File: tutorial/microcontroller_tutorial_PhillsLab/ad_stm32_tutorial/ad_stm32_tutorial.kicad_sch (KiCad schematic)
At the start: 29 parts, among them J1 USB_C_Receptacle_USB2.0_16P, J2 TagConnect_TC2030-NL, J3 Conn_01x06, U2 STM32F042G6Ux, Y2 Crystal_GND24

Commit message: Started PCB Layout of power section
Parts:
- FB1: footprint Inductor_SMD:L_6.3x6.3_H3 -> Inductor_SMD:L_0603_1608Metric
- J3: footprint Connector_JST:JST_XH_S6B-XH-A_1x06_P2.50mm_Horizontal -> Connector_JST:JST_EH_S6B-EH_1x06_P2.50mm_Horizontal
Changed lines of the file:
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@@
 			)
 		)
-		(property "Footprint" "Connector_JST:JST_XH_S6B-XH-A_1x06_P2.50mm_Horizontal"
+		(property "Footprint" "Connector_JST:JST_EH_S6B-EH_1x06_P2.50mm_Horizontal"
 			(at 162.56 157.48 0)
 			(effects
@@
 			)
 		)
-		(property "Footprint" "Inductor_SMD:L_6.3x6.3_H3"
+		(property "Footprint" "Inductor_SMD:L_0603_1608Metric"
 			(at 95.25 33.528 90)
 			(effects

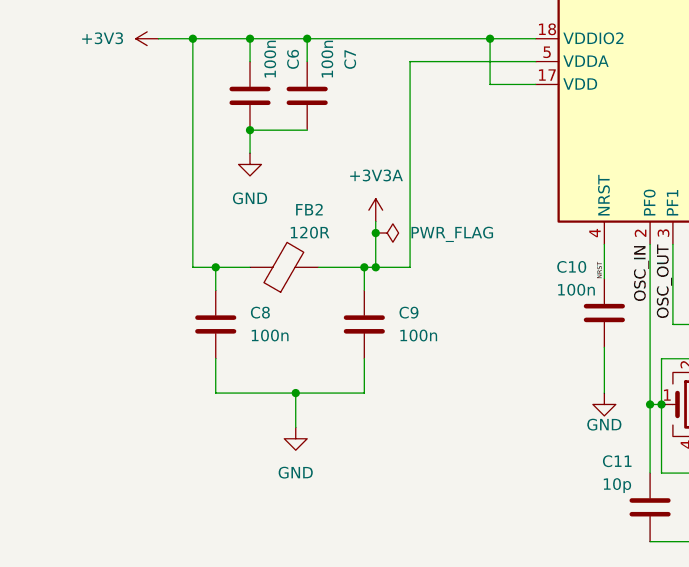
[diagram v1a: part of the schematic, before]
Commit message: Started adding MCU (STM32F4) and it's components
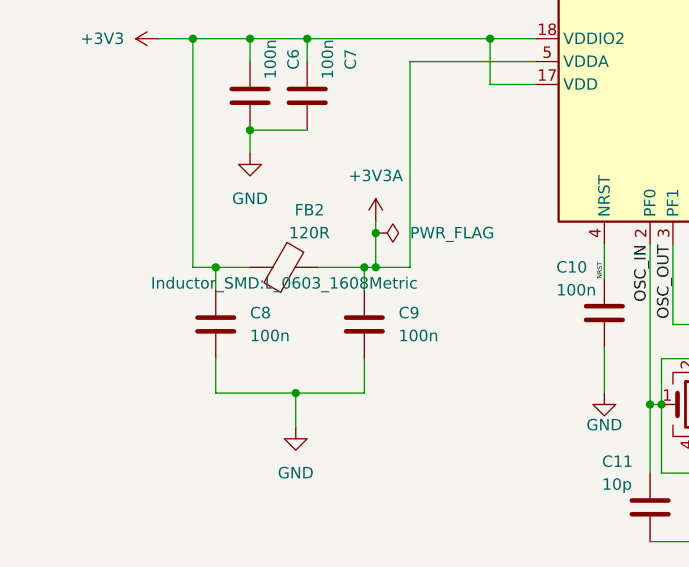
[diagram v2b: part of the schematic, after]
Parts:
- FB2: footprint Inductor_SMD:L_6.3x6.3_H3 -> Inductor_SMD:L_0603_1608Metric
- L1: footprint Inductor_SMD:NRH2412T2R2MNGH -> Inductor_SMD:L_Taiyo-Yuden_NR-24xx
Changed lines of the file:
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@@
 			)
 		)
-		(property "Footprint" "Inductor_SMD:L_6.3x6.3_H3"
+		(property "Footprint" "Inductor_SMD:L_0603_1608Metric"
 			(at 52.07 150.368 90)
 			(effects
@@
 					(size 1.27 1.27)
 				)
-				(hide yes)
 			)
 		)
@@
 			)
 		)
-		(property "Footprint" "Inductor_SMD:NRH2412T2R2MNGH"
+		(property "Footprint" "Inductor_SMD:L_Taiyo-Yuden_NR-24xx"
 			(at 185.42 127.94 0)
 			(effects

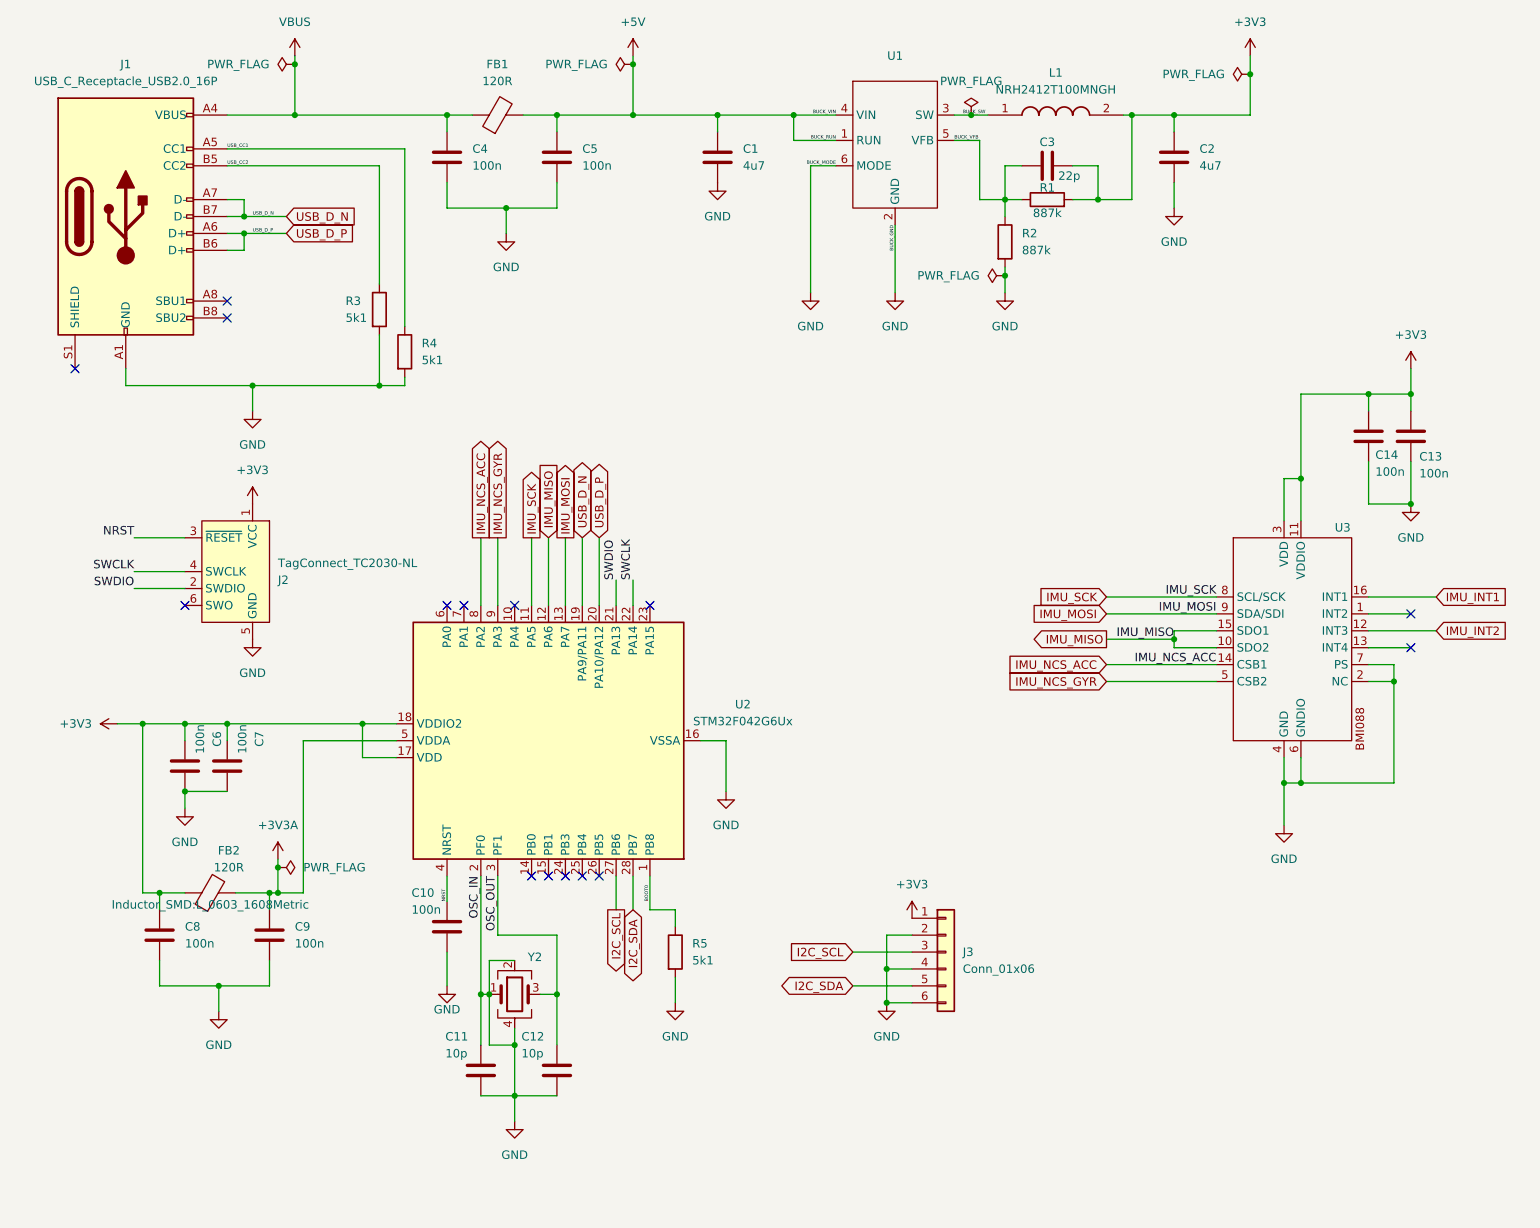
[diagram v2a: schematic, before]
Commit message: Finished placement of all the components
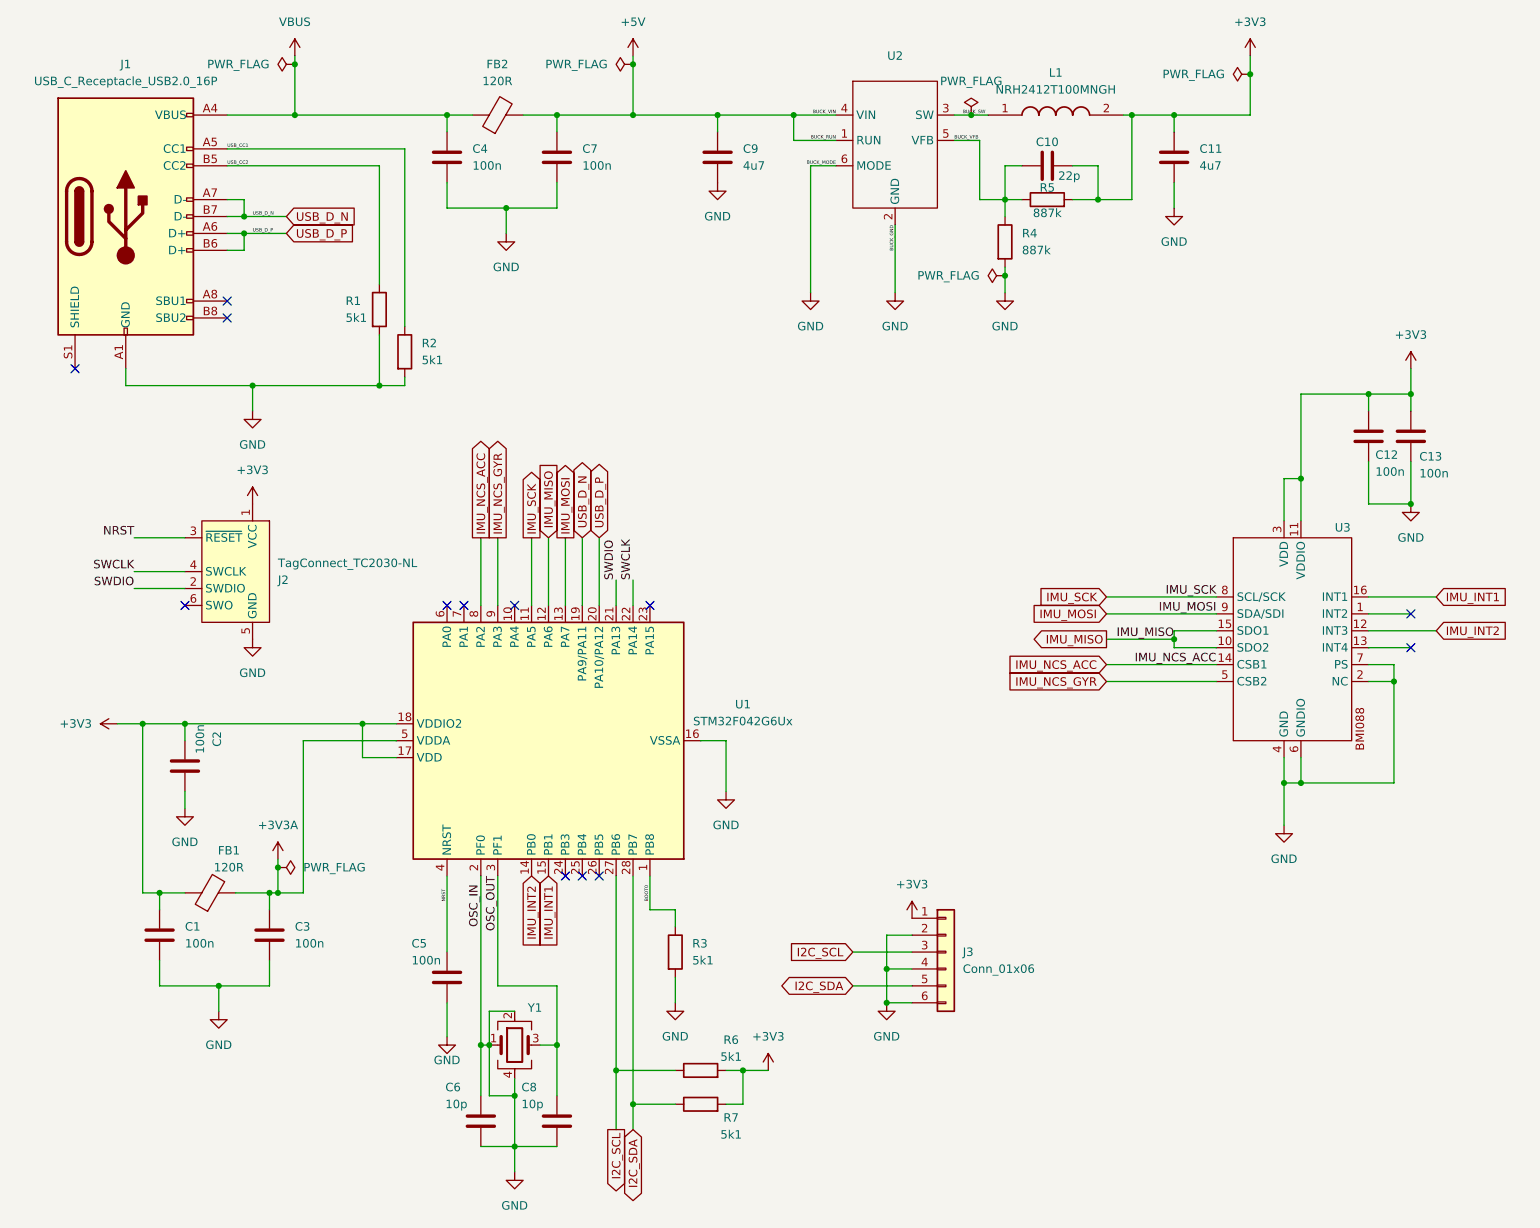
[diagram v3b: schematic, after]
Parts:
- removed C7: 100n, Capacitor_SMD:C_0603_1608Metric, symbol Device:C
- added R6, R7: 5k1, Resistor_SMD:R_0603_1608Metric, symbol Device:R
- J3: footprint Connector_JST:JST_EH_S6B-EH_1x06_P2.50mm_Horizontal -> Connector_JST:JST_GH_SM06B-GHS-TB_1x06-1MP_P1.25mm_Horizontal
- renumbered C8 to C1, C3 to C10, C2 to C11, C14 to C12, C6 to C2, C9 to C3, C10 to C5, C11 to C6, C5 to C7, C12 to C8, C1 to C9, FB2 to FB1, FB1 to FB2, R3 to R1, R4 to R2, R5 to R3, R2 to R4, R1 to R5, U2 to U1, U1 to U2, Y2 to Y1
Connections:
- net +3V3: now also R6.2, R7.2
- net I2C_SCL: now also R6.1
- net I2C_SDA: now also R7.1
- net IMU_INT1: now also U1.15 (PB1)
- net IMU_INT2: now also U1.14 (PB0)
- no-connect marks 15 -> 13
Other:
- moved on the sheet: C5, C6, C8, Y1

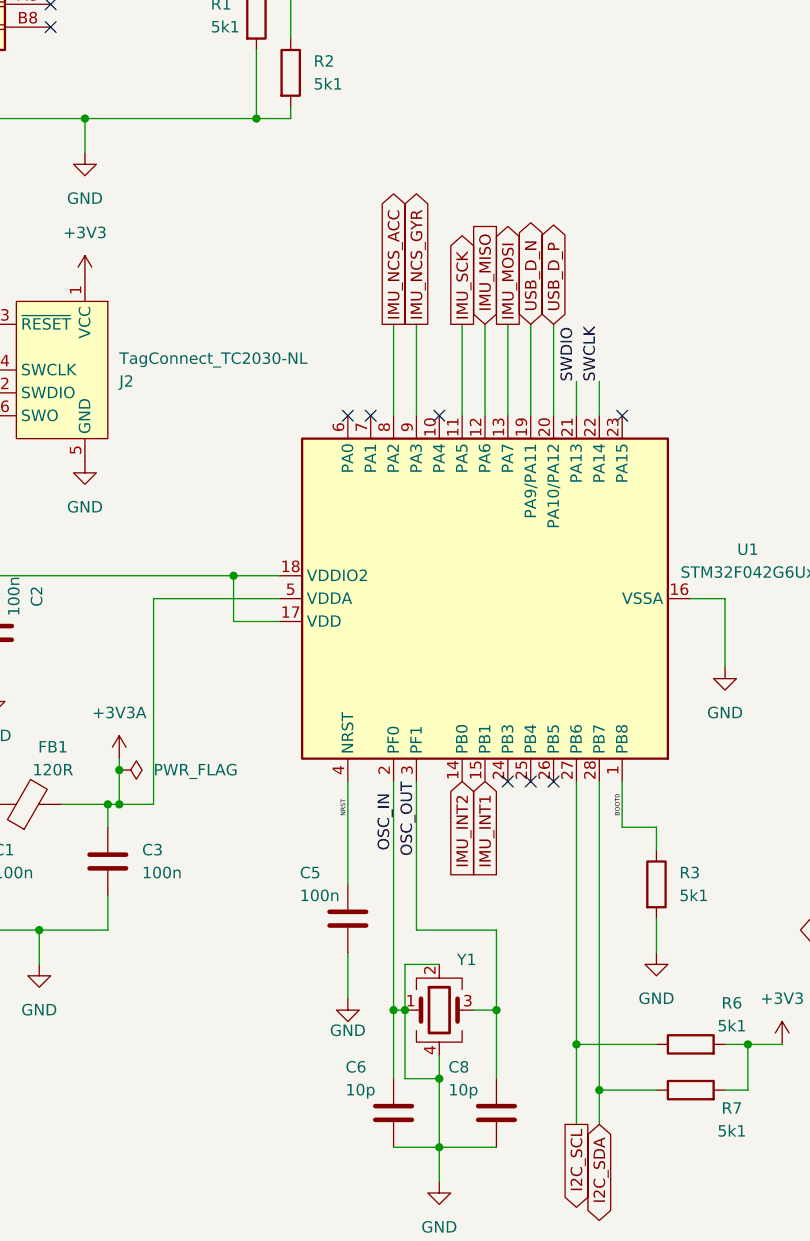
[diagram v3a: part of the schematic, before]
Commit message: Added all the traces and connecting Via's. Check out ViaStitching tool on github
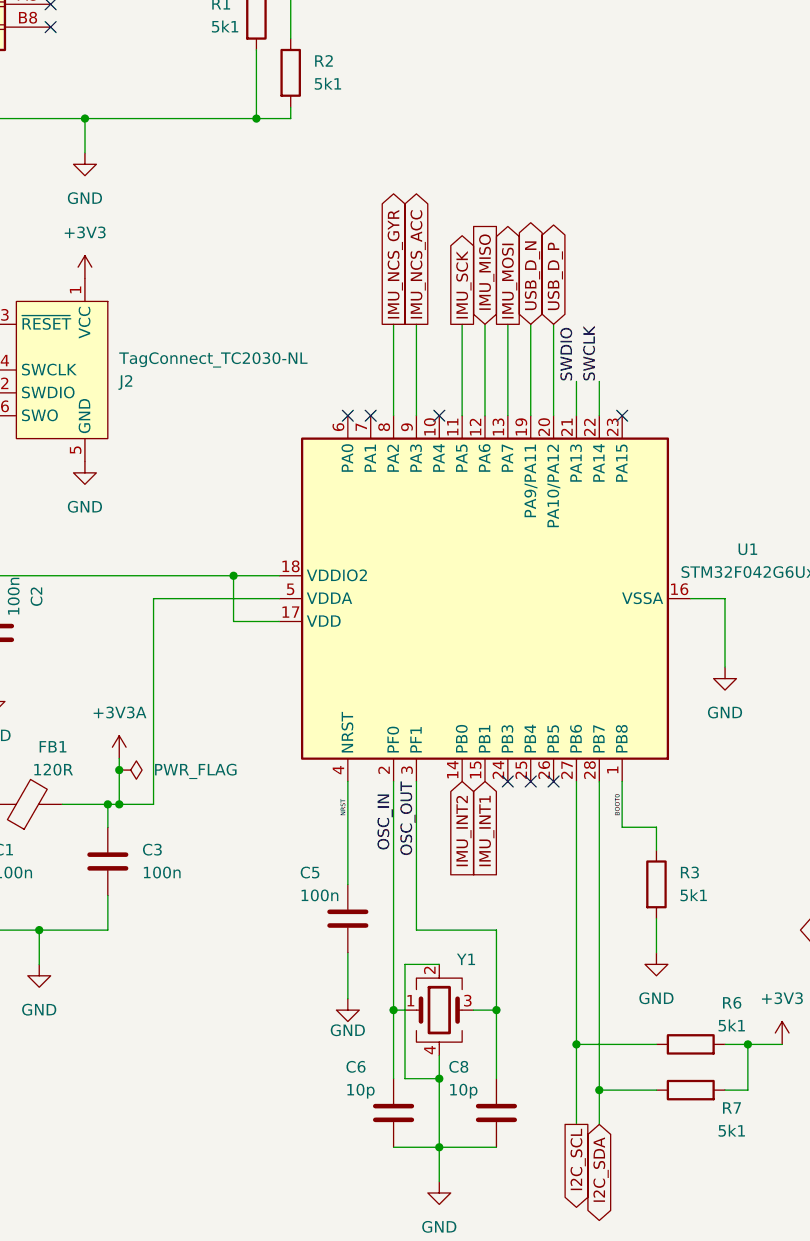
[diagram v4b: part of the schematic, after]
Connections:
- net GND: no longer C6.1, U1.2 (PF0), Y1.1
- net IMU_NCS_ACC: now also U1.9 (PA3); no longer U1.8 (PA2)
- net IMU_NCS_GYR: now also U1.8 (PA2); no longer U1.9 (PA3)
- new net OSC_IN: C6.1, U1.2 (PF0), Y1.1
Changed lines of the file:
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@@
-	)
-	(junction
-		(at 93.98 171.45)
-		(diameter 0)
-		(color 0 0 0 0)
 	)
 	(junction
@@
 	(wire
 		(pts
-			(xy 93.98 171.45) (xy 93.98 179.07)
+			(xy 93.98 166.37) (xy 93.98 179.07)
 		)
 		(stroke
@@
 		(pts
 			(xy 186.69 114.3) (xy 203.2 114.3)
-		)
-		(stroke
-			(width 0)
-			(type default)
-		)
-	)
-	(wire
-		(pts
-			(xy 93.98 166.37) (xy 93.98 171.45)
 		)
 		(stroke
@@
 		)
 	)
-	(global_label "IMU_NCS_GYR"
+	(global_label "IMU_MOSI"
+		(shape input)
+		(at 186.69 106.68 180)
+		(fields_autoplaced yes)
+		(effects
+			(font
+				(size 1.27 1.27)
+			)
+			(justify right)
+		)
+		(property "Intersheetrefs" "${INTERSHEET_REFS}"
+			(at 174.7543 106.68 0)
+			(effects
+				(font
+					(size 1.27 1.27)
+				)
+				(justify right)
+				(hide yes)
+			)
+		)
+	)
+	(global_label "IMU_INT1"
+		(shape input)
+		(at 236.22 104.14 0)
+		(fields_autoplaced yes)
+		(effects
+			(font
+				(size 1.27 1.27)
+			)
+			(justify left)
+		)
+		(property "Intersheetrefs" "${INTERSHEET_REFS}"
+			(at 247.6719 104.14 0)
+			(effects
+				(font
+					(size 1.27 1.27)
+				)
+				(justify left)
+				(hide yes)
+			)
+		)
+	)
+	(global_label "IMU_SCK"
+		(shape output)
+		(at 100.33 95.25 90)
+		(fields_autoplaced yes)
+		(effects
+			(font
+				(size 1.27 1.27)
+			)
+			(justify left)
+		)
+		(property "Intersheetrefs" "${INTERSHEET_REFS}"
+			(at 100.33 84.161 90)
+			(effects
+				(font
+					(size 1.27 1.27)
+				)
+				(justify left)
+				(hide yes)
+			)
+		)
+	)
+	(global_label "USB_D_N"
+		(shape bidirectional)
+		(at 107.95 95.25 90)
+		(fields_autoplaced yes)
+		(effects
+			(font
+				(size 1.27 1.27)
+			)
+			(justify left)
+		)
+		(property "Intersheetrefs" "${INTERSHEET_REFS}"
+			(at 107.95 82.8078 90)
+			(effects
+				(font
+					(size 1.27 1.27)
+				)
+				(justify left)
+				(hide yes)
+			)
+		)
+	)
+	(global_label "I2C_SCL"
+		(shape input)
+		(at 148.59 157.48 180)
+		(fields_autoplaced yes)
+		(effects
+			(font
+				(size 1.27 1.27)
+			)
+			(justify right)
+		)
+		(property "Intersheetrefs" "${INTERSHEET_REFS}"
+			(at 138.0453 157.48 0)
+			(effects
+				(font
+					(size 1.27 1.27)
+				)
+				(justify right)
+				(hide yes)
+			)
+		)
+	)
+	(global_label "IMU_NCS_ACC"
 		(shape output)
 		(at 95.25 95.25 90)
@@
 		)
 	)
-	(global_label "IMU_MOSI"
-		(shape input)
-		(at 186.69 106.68 180)
-		(fields_autoplaced yes)
-		(effects
-			(font
-				(size 1.27 1.27)
-			)
-			(justify right)
-		)
-		(property "Intersheetrefs" "${INTERSHEET_REFS}"
-			(at 174.7543 106.68 0)
-			(effects
-				(font
-					(size 1.27 1.27)
-				)
-				(justify right)
-				(hide yes)
-			)
-		)
-	)
-	(global_label "IMU_INT1"
-		(shape input)
-		(at 236.22 104.14 0)
-		(fields_autoplaced yes)
-		(effects
-			(font
-				(size 1.27 1.27)
-			)
-			(justify left)
-		)
-		(property "Intersheetrefs" "${INTERSHEET_REFS}"
-			(at 247.6719 104.14 0)
-			(effects
-				(font
-					(size 1.27 1.27)
-				)
-				(justify left)
-				(hide yes)
-			)
-		)
-	)
-	(global_label "IMU_SCK"
-		(shape output)
-		(at 100.33 95.25 90)
-		(fields_autoplaced yes)
-		(effects
-			(font
-				(size 1.27 1.27)
-			)
-			(justify left)
-		)
-		(property "Intersheetrefs" "${INTERSHEET_REFS}"
-			(at 100.33 84.161 90)
-			(effects
-				(font
-					(size 1.27 1.27)
-				)
-				(justify left)
-				(hide yes)
-			)
-		)
-	)
-	(global_label "USB_D_N"
-		(shape bidirectional)
-		(at 107.95 95.25 90)
-		(fields_autoplaced yes)
-		(effects
-			(font
-				(size 1.27 1.27)
-			)
-			(justify left)
-		)
-		(property "Intersheetrefs" "${INTERSHEET_REFS}"
-			(at 107.95 82.8078 90)
-			(effects
-				(font
-					(size 1.27 1.27)
-				)
-				(justify left)
-				(hide yes)
-			)
-		)
-	)
-	(global_label "I2C_SCL"
-		(shape input)
-		(at 148.59 157.48 180)
-		(fields_autoplaced yes)
-		(effects
-			(font
-				(size 1.27 1.27)
-			)
-			(justify right)
-		)
-		(property "Intersheetrefs" "${INTERSHEET_REFS}"
-			(at 138.0453 157.48 0)
-			(effects
-				(font
-					(size 1.27 1.27)
-				)
-				(justify right)
-				(hide yes)
-			)
-		)
-	)
 	(global_label "I2C_SDA"
 		(shape bidirectional)
@@
 	)
 	(global_label "IMU_NCS_ACC"
+		(shape input)
+		(at 186.69 114.3 180)
+		(fields_autoplaced yes)
+		(effects
+			(font
+				(size 1.27 1.27)
+			)
+			(justify right)
+		)
+		(property "Intersheetrefs" "${INTERSHEET_REFS}"
+			(at 170.9443 114.3 0)
+			(effects
+				(font
+					(size 1.27 1.27)
+				)
+				(justify right)
+				(hide yes)
+			)
+		)
+	)
+	(global_label "IMU_NCS_GYR"
 		(shape output)
 		(at 92.71 95.25 90)
@@
 				(hide yes)
 			)
-		)
-	)
-	(global_label "IMU_NCS_ACC"
-		(shape input)
-		(at 186.69 114.3 180)
-		(fields_autoplaced yes)
-		(effects
-			(font
-				(size 1.27 1.27)
-			)
-			(justify right)
-		)
-		(property "Intersheetrefs" "${INTERSHEET_REFS}"
-			(at 170.9443 114.3 0)
-			(effects
-				(font
-					(size 1.27 1.27)
-				)
-				(justify right)
-				(hide yes)
-			)
